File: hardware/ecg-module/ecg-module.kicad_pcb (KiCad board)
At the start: 2 copper layers, 58 x 58 mm, 46 parts, among them IC1 AP2112K-1.8TRG1, J1 35RASMT2BHNTRX, J2 LEFT-UI, J3 RIGHT-UI, U1 MAX30003CTI, U2 TXB0108PWR, Y1 KX3211A0032.768000

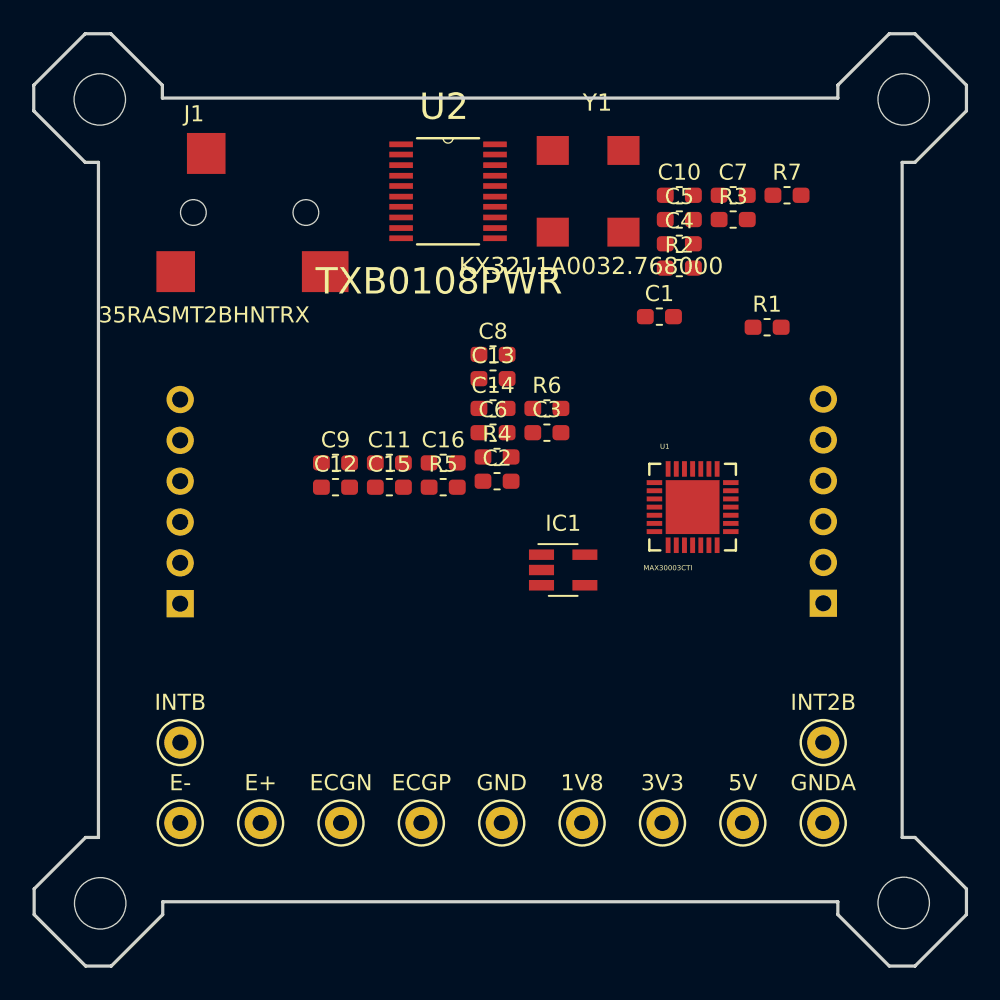
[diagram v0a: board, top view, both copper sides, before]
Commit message: Put footprints in right place
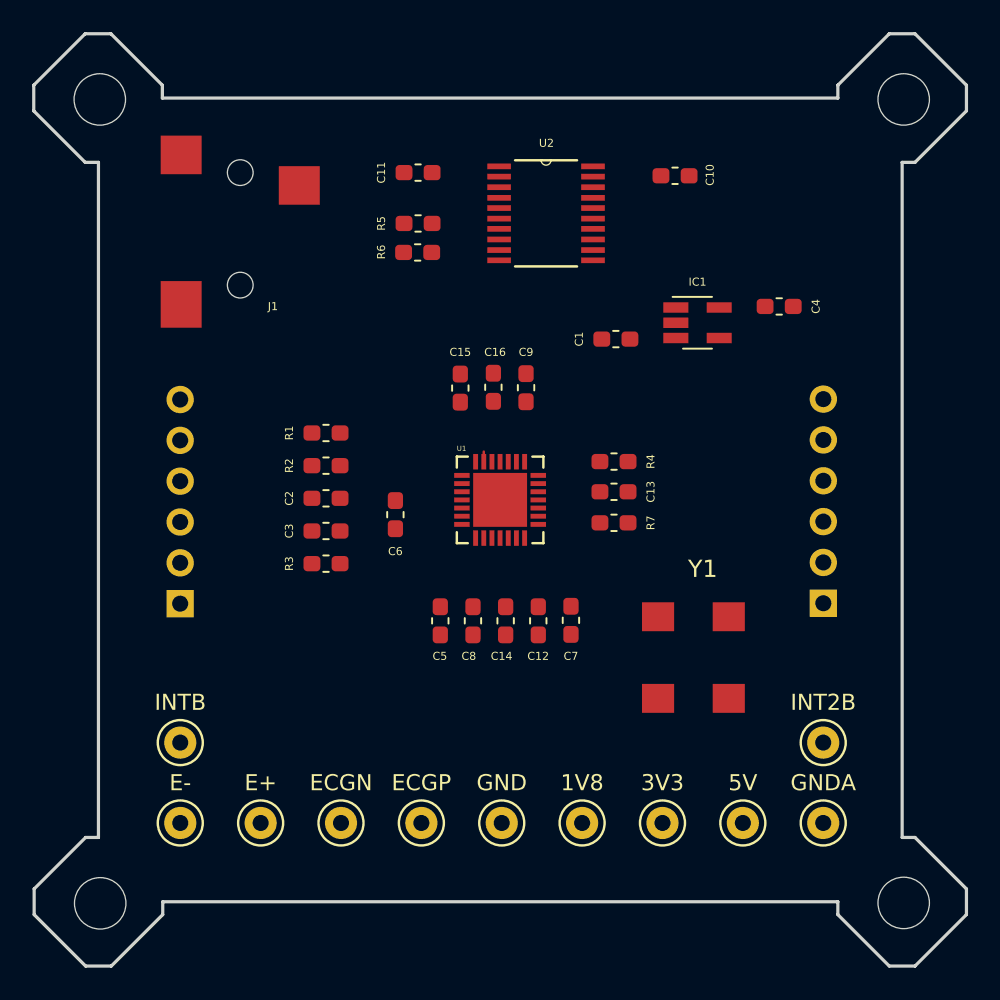
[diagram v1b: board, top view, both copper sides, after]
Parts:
- J1: value 35RASMT2BHNTRX -> (none)
- U1: value MAX30003CTI -> (none)
- U2: value TXB0108PWR -> (none)
- Y1: value KX3211A0032.768000 -> (none)
- moved R3 33.2 mm to (137.7, 109.0), turned to 180 degrees
- moved Y1 29.7 mm to (160.5, 114.8)
- moved C5 29.1 mm to (144.8, 112.5), turned to 90 degrees
- moved C7 28.3 mm to (152.9, 112.5), turned to 270 degrees
- moved R1 28.2 mm to (137.7, 100.8), turned to 180 degrees
- moved R2 25.2 mm to (137.7, 102.9), turned to 180 degrees
- moved R7 23.0 mm to (155.6, 106.4)
- moved C11 18.1 mm to (143.4, 84.6)
- moved IC1 17.5 mm to (160.8, 94.0)
- moved C8 16.6 mm to (146.8, 112.5), turned to 270 degrees
- moved R5 16.5 mm to (143.4, 87.8)
- moved C12 15.1 mm to (150.9, 112.5), turned to 270 degrees
- moved C3 15.0 mm to (137.7, 106.9), turned to 180 degrees
- moved C14 13.2 mm to (148.8, 112.5), turned to 270 degrees
- moved C9 12.7 mm to (150.1, 98.0), turned to 90 degrees
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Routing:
- net Net-(C15-Pad1): track 0.00 -> 0.63 mm
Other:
- net class PWR added: clearance 0.2032, trace_width 0.2032, via_dia 0.6, via_drill 0.3
- net class SIG added: clearance 0.1524, trace_width 0.1524, via_dia 0.6, via_drill 0.3
- rule trace_min: 0.2 -> 0.1524
- rule via_min_size: 0.4 -> 0.6

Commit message: Add GND and GNDA routing
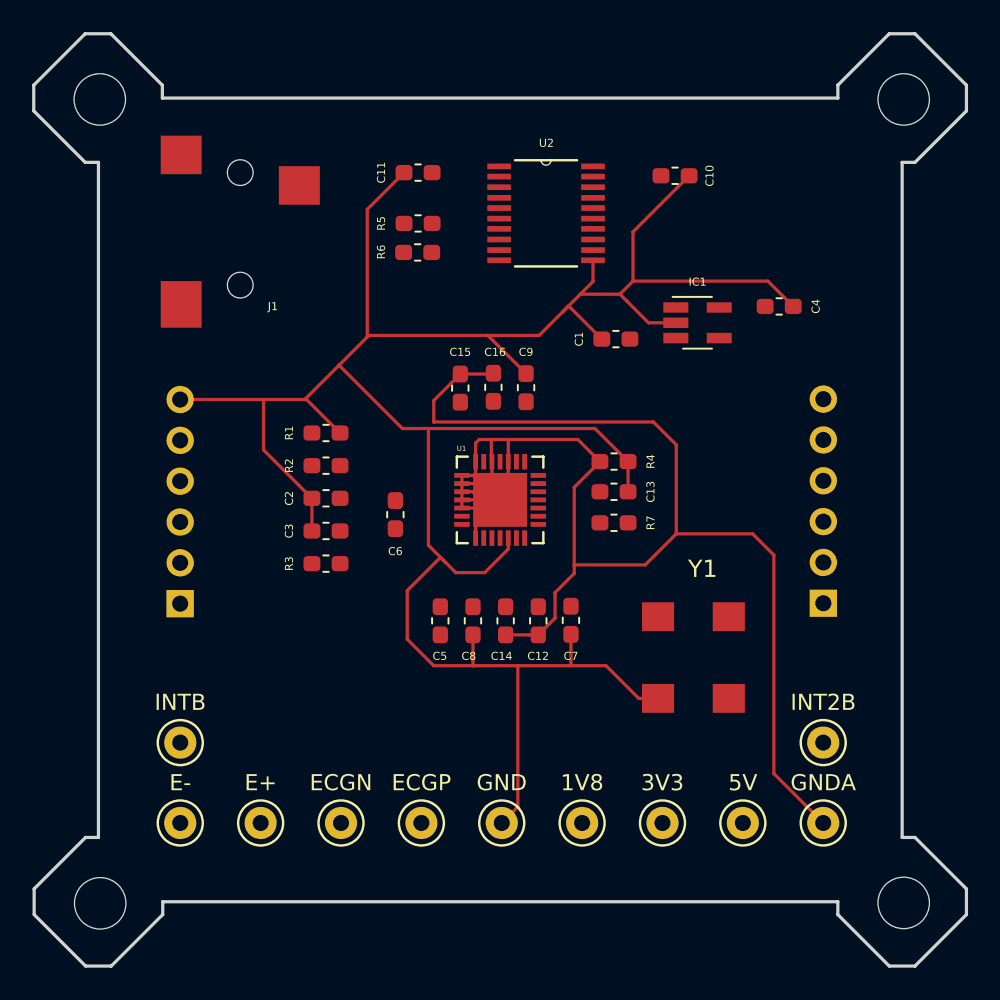
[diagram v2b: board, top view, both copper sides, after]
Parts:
- turned C10 to 180 degrees
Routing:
- net GND: track 0.00 -> 160.9 mm
- net GNDA: track 0.00 -> 112.0 mm
- net Net-(C15-Pad1): track 0.63 -> 0.00 mm

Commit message: Add basic routing
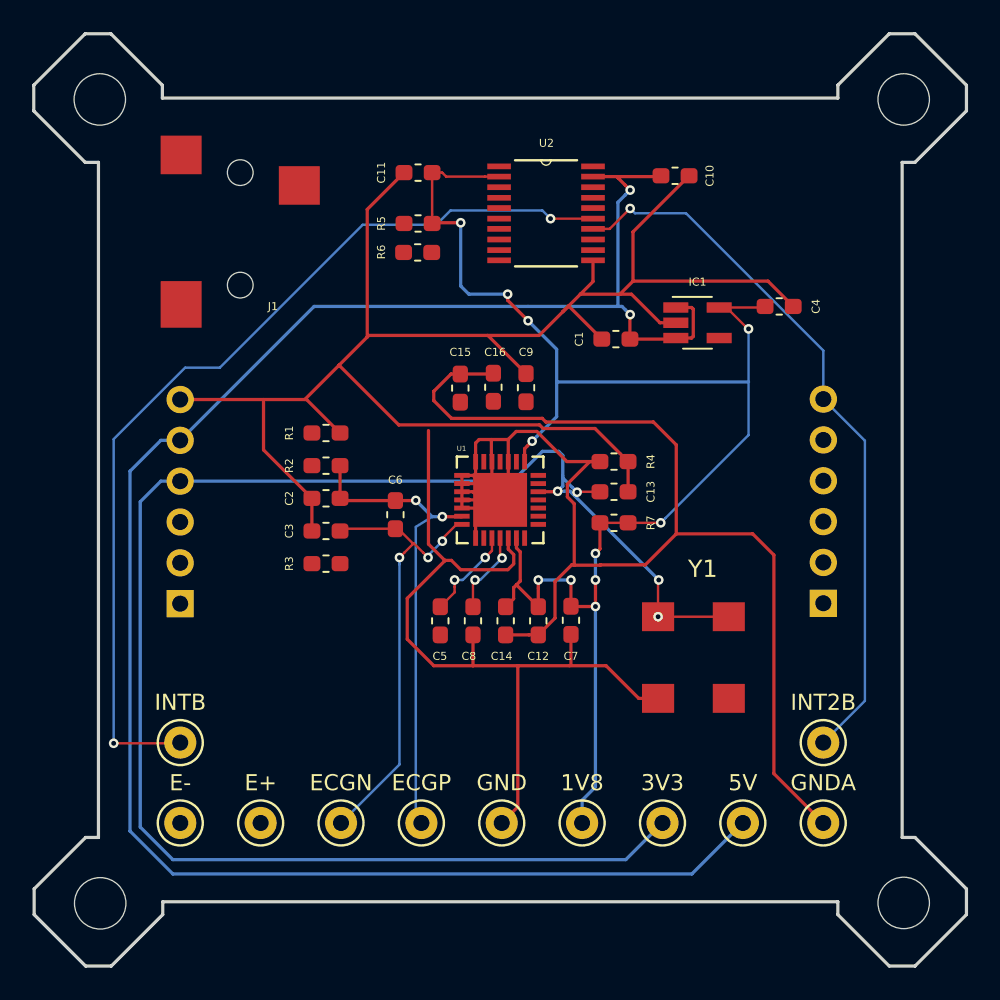
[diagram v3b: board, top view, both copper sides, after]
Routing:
- net +5V: track 0.00 -> 119.8 mm, vias 0 -> 2
- net +3V3: track 0.00 -> 103.7 mm, vias 0 -> 4
- net +1V8: track 0.05 -> 96.8 mm, vias 0 -> 11
- net INTB_5V: track 0.00 -> 59.0 mm, vias 0 -> 2
- net INT2B_5V: track 0.00 -> 45.1 mm, vias 0 -> 1
- net Net-(C2-Pad2): track 0.00 -> 29.1 mm, vias 0 -> 2
- net Net-(C3-Pad1): track 0.00 -> 28.7 mm, vias 0 -> 3
- net Net-(C5-Pad2): track 0.00 -> 5.90 mm, vias 0 -> 2
- net Net-(C8-Pad1): track 0.00 -> 5.26 mm, vias 0 -> 2

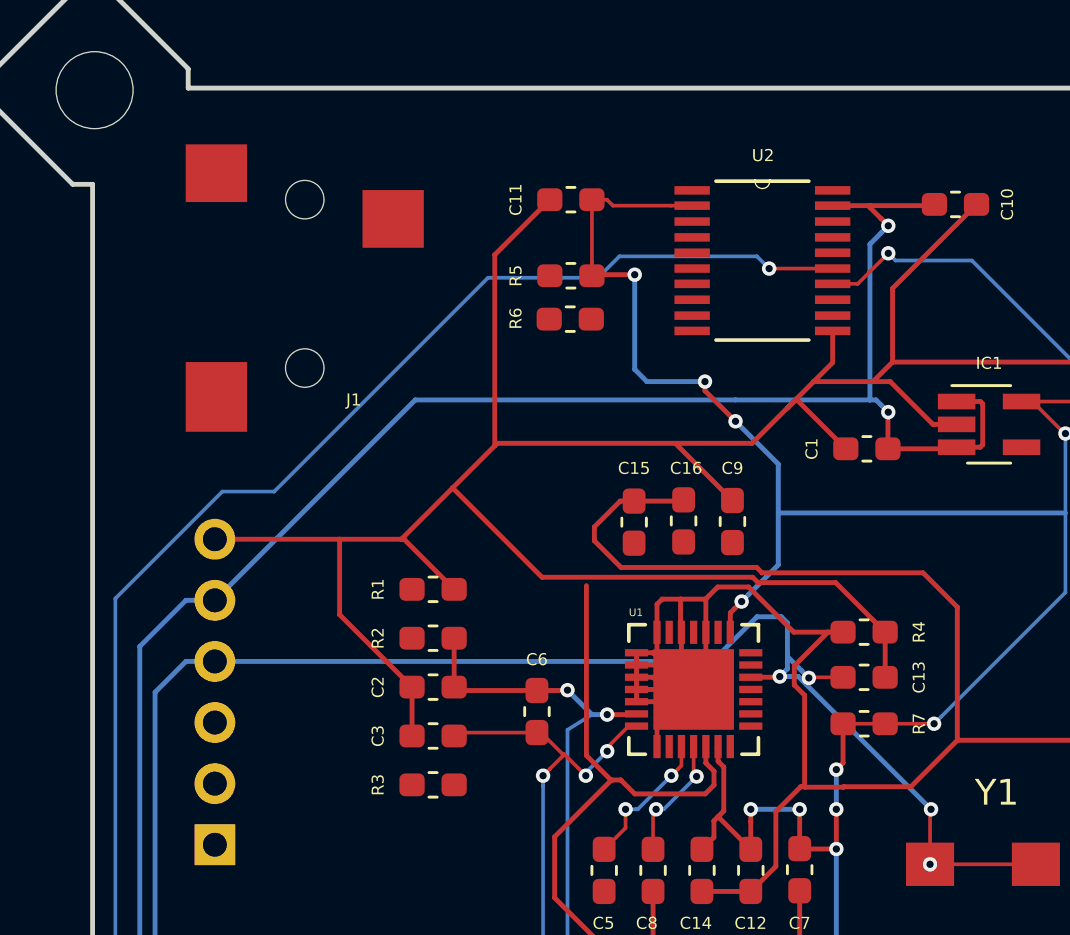
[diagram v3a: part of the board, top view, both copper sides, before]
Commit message: Update footprint to screw terminal
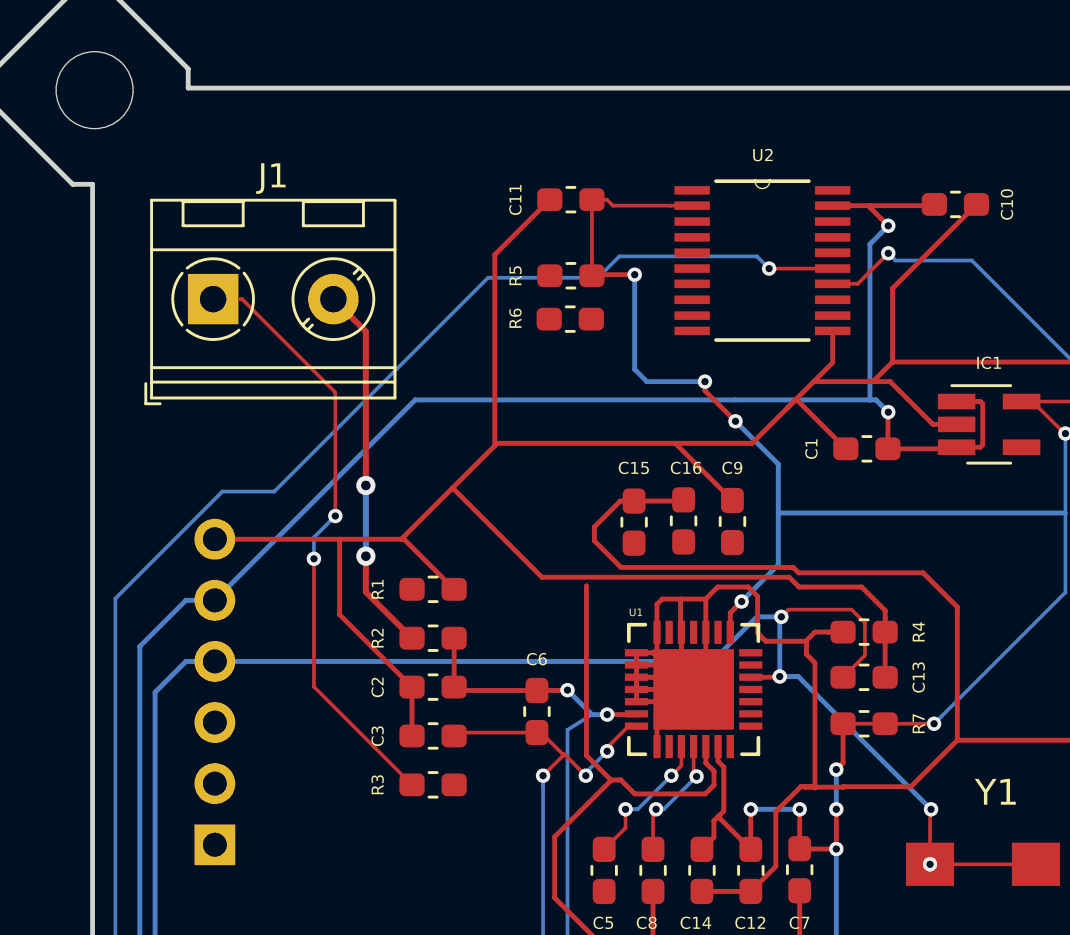
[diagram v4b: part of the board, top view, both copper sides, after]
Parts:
- J1: value (none) -> ST_01x02; footprint SWITCHCRAFT:SWITCHCRAFT_35RASMT2BHNTRX -> TerminalBlock_RND:TerminalBlock_RND_205-00045_1x02_P5.00mm_Horizontal
- moved J1 3.86 mm to (128.5, 88.8), turned to 0 degrees
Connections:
- IC1 pad 4: (no net) -> Net-(IC1-Pad4)
- J2 pad 1: (no net) -> Net-(J2-Pad1)
- J2 pad 2: (no net) -> Net-(J2-Pad2)
- J2 pad 3: (no net) -> Net-(J2-Pad3)
- R1 pad 2: Net-(J1-Pad5) -> Net-(J1-Pad1)
- R2 pad 2: Net-(J1-Pad1) -> Net-(J1-Pad2)
- R3 pad 2: Net-(J1-Pad4) -> Net-(J1-Pad1)
- U2 pad 12: (no net) -> Net-(U2-Pad12)
- U2 pad 13: (no net) -> Net-(U2-Pad13)
- U2 pad 8: (no net) -> Net-(U2-Pad8)
- U2 pad 9: (no net) -> Net-(U2-Pad9)
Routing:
- net Net-(J1-Pad1): track 0.00 -> 25.1 mm, vias 0 -> 2
- net Net-(J1-Pad2): track 0.00 -> 15.5 mm, vias 0 -> 2
- net +3V3: track 103.7 -> 107.3 mm
- net GNDA: track 112.1 -> 112.9 mm
- net GND: track 161.3 -> 161.8 mm

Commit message: Update routing
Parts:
- removed R1: 0R, Resistor_SMD:R_0603_1608Metric_Pad1.05x0.95mm_HandSolder
- moved ? 0.08 mm to (173.5, 80.1)
- moved ? 0.05 mm to (123.6, 130.1)
- renumbered 5V to TP1, INTB to TP10, INT2B to TP11, 3V3 to TP2, 1V8 to TP3, ECGN to TP4, ECGP to TP5, E- to TP6, E+ to TP7, GND to TP8, GNDA to TP9
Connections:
- IC1 pad 4: Net-(IC1-Pad4) -> (no net)
- J2 pad 1: Net-(J2-Pad1) -> (no net)
- J2 pad 2: Net-(J2-Pad2) -> (no net)
- J2 pad 3: Net-(J2-Pad3) -> (no net)
- TP6 pad 1: Net-(J1-Pad4) -> Net-(J1-Pad1)
- TP7 pad 1: Net-(J1-Pad1) -> Net-(J1-Pad2)
- U2 pad 12: Net-(U2-Pad12) -> (no net)
- U2 pad 13: Net-(U2-Pad13) -> (no net)
- U2 pad 8: Net-(U2-Pad8) -> (no net)
- U2 pad 9: Net-(U2-Pad9) -> (no net)
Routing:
- net GND: track 161.8 -> 0.00 mm
- net INTB_5V: track 59.0 -> 135.1 mm
- net CSB_5V: track 0.00 -> 65.6 mm
- net SCLK_5V: track 0.00 -> 60.2 mm
- net MOSI_5V: track 0.00 -> 54.8 mm
- net +5V: track 119.8 -> 74.2 mm, vias 2 -> 0
- net MISO_5V: track 0.00 -> 42.9 mm
- net SCLK_1.8V: track 0.00 -> 28.5 mm, vias 0 -> 4
- net CSB_1.8V: track 0.00 -> 27.6 mm, vias 0 -> 4
- net MISO_1.8V: track 0.00 -> 26.6 mm, vias 0 -> 2
- net Net-(J1-Pad2): track 15.5 -> 41.5 mm
- net MOSI_1.8V: track 0.00 -> 25.5 mm, vias 0 -> 2
- net Net-(J1-Pad1): track 25.1 -> 47.2 mm
- net INT2B_1.8V: track 0.00 -> 20.7 mm, vias 0 -> 2
- net INTB_1.8V: track 0.00 -> 19.6 mm, vias 0 -> 4
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
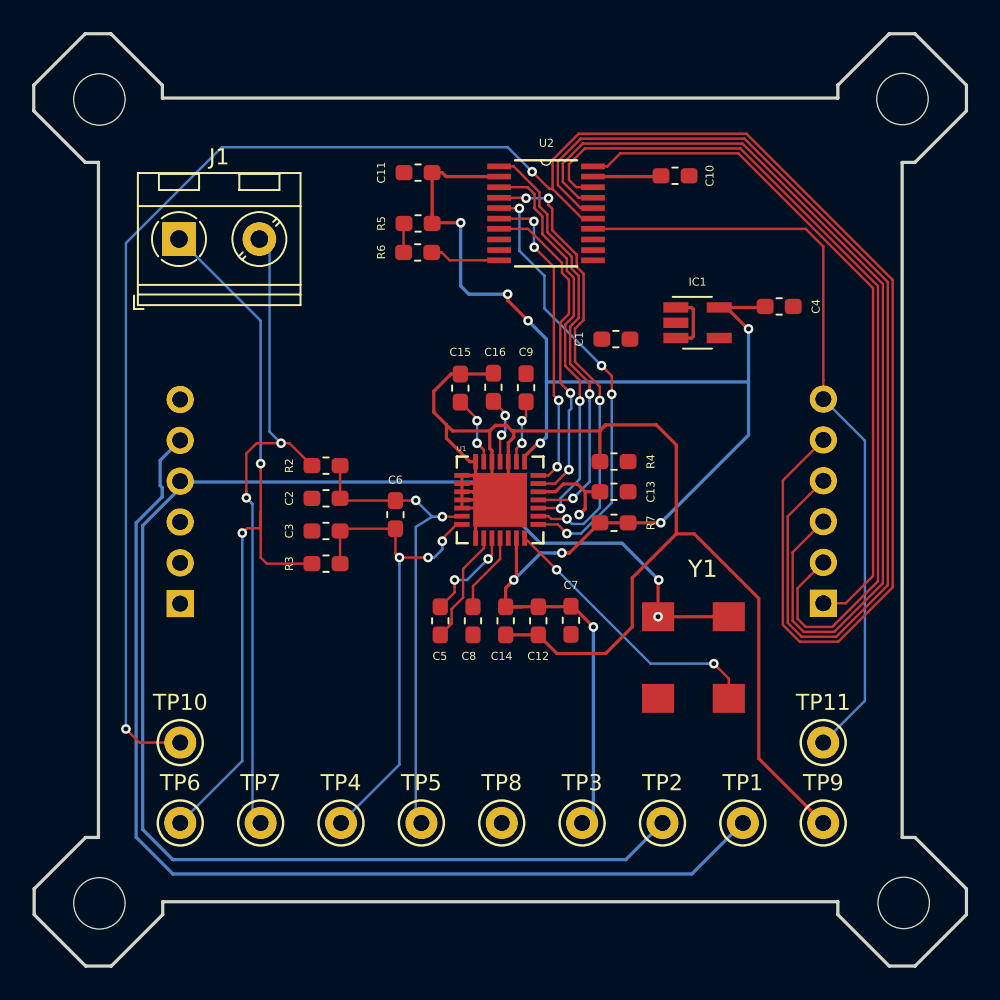
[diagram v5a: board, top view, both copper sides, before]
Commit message: Complete all connections route
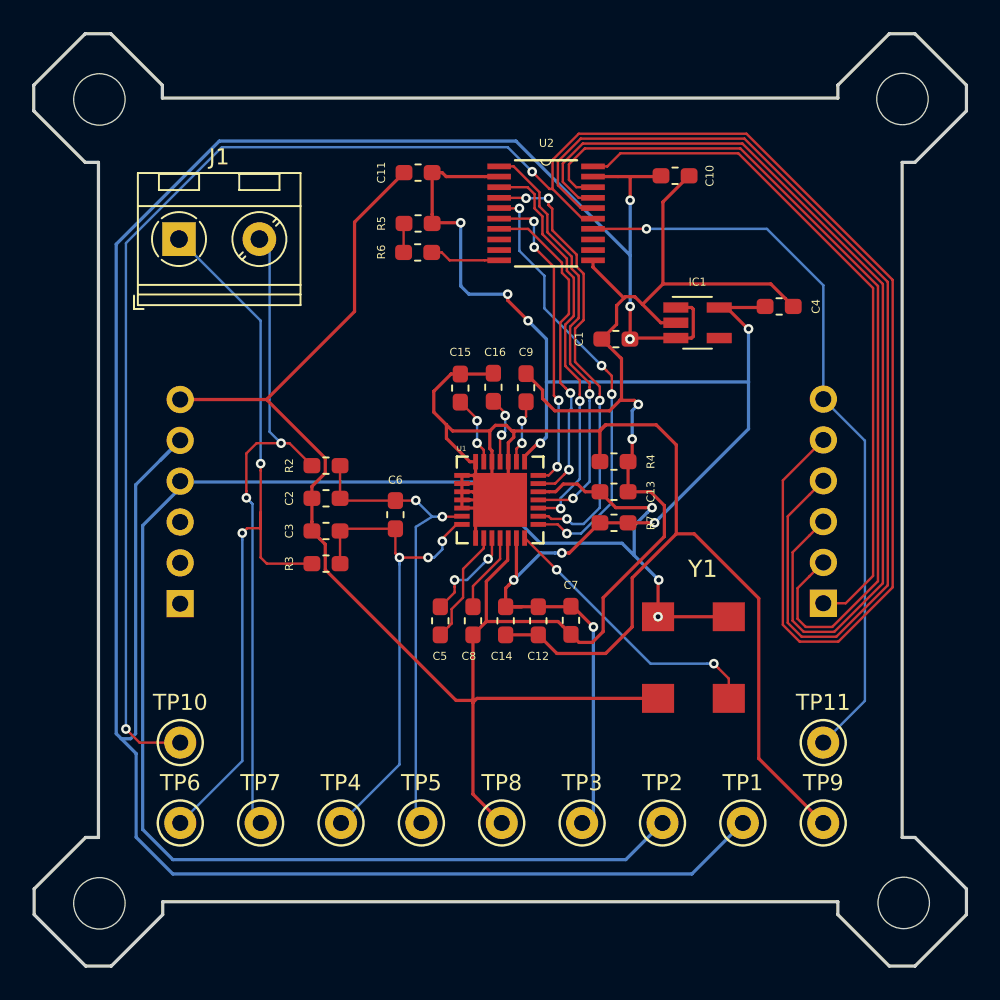
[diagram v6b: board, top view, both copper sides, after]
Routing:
- net GND: track 0.00 -> 146.3 mm, vias 0 -> 2
- net +5V: track 74.2 -> 158.5 mm, vias 0 -> 3
- net +3V3: track 101.3 -> 106.8 mm
- net INT2B_5V: track 47.8 -> 46.4 mm, vias 0 -> 1
